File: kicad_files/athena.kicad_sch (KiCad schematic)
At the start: 618 parts, among them J1 TYPE-C-31-M-12, J2 A1001WR-S-04P, Q1 2N7002, Q2 2N7002, Q3 AO3401A, Q4 2N7002, Q5 2N7002, Q6 2N7002, Q7 2N7002, Q8 2N7002, SW1 K2-1187SQ-A4SW-06, SW10 MX Switch, SW100 MX Switch, SW101 MX Switch, SW102 MX Switch, SW103 MX Switch, SW104 MX Switch, SW105 MX Switch, SW106 MX Switch, SW107 MX Switch, SW108 MX Switch, SW109 MX Switch, SW11 MX Switch, SW110 MX Switch, SW111 MX Switch, SW112 MX Switch, SW113 MX Switch, SW114 MX Switch, SW115 MX Switch, SW116 MX Switch, SW117 MX Switch, SW118 MX Switch, SW119 MX Switch, SW12 MX Switch, SW120 MX Switch, SW13 MX Switch, SW14 MX Switch, SW15 MX Switch, SW16 MX Switch, SW17 MX Switch, SW18 MX Switch, SW19 MX Switch, SW2 MX Switch, SW20 MX Switch, SW21 MX Switch, SW22 MX Switch, SW23 MX Switch, SW24 MX Switch, SW25 MX Switch, SW26 MX Switch, SW27 MX Switch, SW28 MX Switch, SW29 MX Switch, SW3 MX Switch, SW30 MX Switch, SW31 MX Switch, SW32 MX Switch, SW33 MX Switch, SW34 MX Switch, SW35 MX Switch, SW36 MX Switch, SW37 MX Switch, SW38 MX Switch, SW39 MX Switch, SW4 MX Switch, SW40 MX Switch, SW41 MX Switch, SW42 MX Switch, SW43 MX Switch, SW44 MX Switch, SW45 MX Switch, SW46 MX Switch, SW47 MX Switch, SW48 MX Switch, SW49 MX Switch, SW5 MX Switch, SW50 MX Switch, SW51 MX Switch, SW52 MX Switch, SW53 MX Switch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

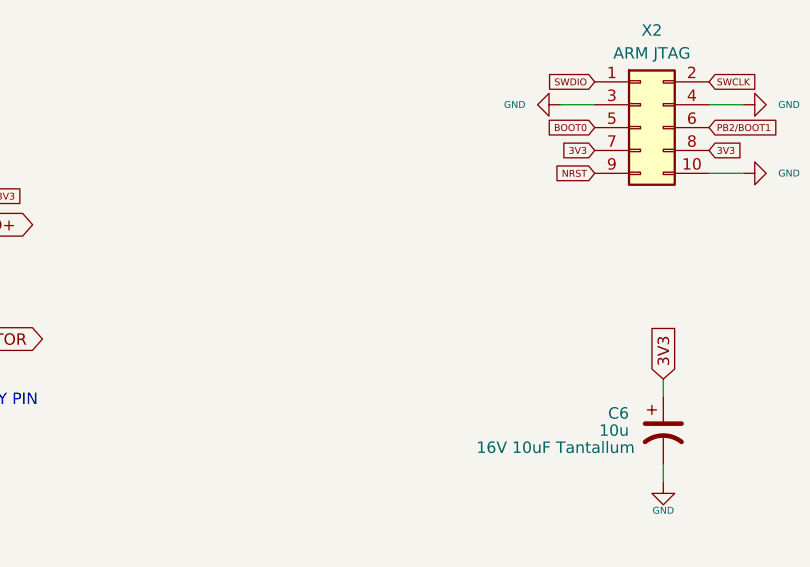
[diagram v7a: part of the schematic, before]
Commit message: Update USB tracing for new trace sizes, crystal GND pads are solid
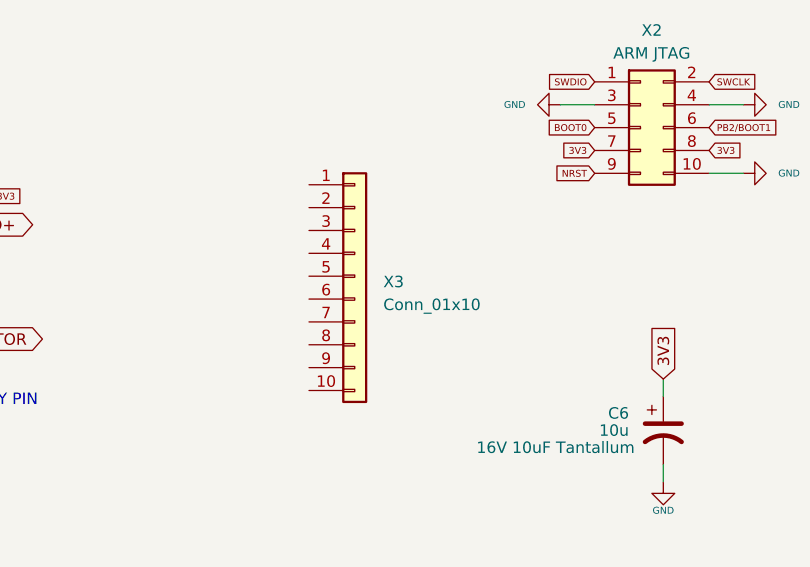
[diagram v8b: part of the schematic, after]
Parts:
- added X3: Conn_01x10, acheron_Connectors:PinHeader_1x10_P2.54mm_Vertical, symbol Connector_Generic:Conn_01x10
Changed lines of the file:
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@@
+    )
+  )
+  (symbol (lib_id "Connector_Generic:Conn_01x10") (at 367.665 77.47 0) (unit 1)
+    (in_bom no) (on_board yes) (dnp no) (fields_autoplaced)
+    (property "Reference" "X3" (at 370.84 78.105 0)
+      (effects (font (size 1.27 1.27)) (justify left))
+    )
+    (property "Value" "Conn_01x10" (at 370.84 80.645 0)
+      (effects (font (size 1.27 1.27)) (justify left))
+    )
+    (property "Footprint" "acheron_Connectors:PinHeader_1x10_P2.54mm_Vertical" (at 367.665 77.47 0)
+      (effects (font (size 1.27 1.27)) hide)
+    )
+    (property "Datasheet" "~" (at 367.665 77.47 0)
+      (effects (font (size 1.27 1.27)) hide)
+    )
+    (property "Package" "" (at 367.665 77.47 0)
+      (effects (font (size 1.27 1.27)) hide)
+    )
+    (property "Manufacturer" "" (at 367.665 77.47 0)
+      (effects (font (size 1.27 1.27)) hide)
+    )
+    (property "Manufacturer Part Number" "" (at 367.665 77.47 0)
+      (effects (font (size 1.27 1.27)) hide)
+    )
+    (property "Vendor Part Number" "" (at 367.665 77.47 0)
+      (effects (font (size 1.27 1.27)) hide)
+    )
+    (property "Specification" "" (at 367.665 77.47 0)
+      (effects (font (size 1.27 1.27)) hide)
+    )
+    (pin "1")
+    (pin "10")
+    (pin "2")
+    (pin "3")
+    (pin "4")
+    (pin "5")
+    (pin "6")
+    (pin "7")
+    (pin "8")
+    (pin "9")
+    (instances
+      (project "athena"
+        (path "/9ce6b20d-0a6c-402a-b232-5eafd6242eb3"
+          (reference "X3") (unit 1)
+        )
+      )
     )
   )
